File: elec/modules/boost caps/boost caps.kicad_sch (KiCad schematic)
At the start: 9 parts, among them J1 Conn_01x05, J2 Conn_01x05, U1 LM2587S-ADJ

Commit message: did boost without caps for now might have to re config stitch vias pos
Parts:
- removed J1, J2: Conn_01x05, Pinheaders:PinHeader_1x05_P2.54mm_Vertical, symbol Connector_Generic:Conn_01x05
- added C35: 0.1uF, Capacitor_SMD:C_0603_1608Metric, symbol Device:C
- added C36: 100uF, Capacitor_THT:CP_Radial_D8.0mm_P3.50mm, symbol Device:C_Polarized
- added C37, C38, C39, C41, C42, C43: 1000uF, Capacitor_THT:CP_Radial_D16.0mm_P7.50mm, symbol Device:C_Polarized
- added J1, J2, J3: Conn_01x01_Pin, cool custom thingy:custompadfat, symbol Connector:Conn_01x01_Pin
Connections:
- net +12V: now also C35.1, C36.1, J1.1 (Pin_1)
- net +24V: now also C37.1, C38.1, C39.1, C41.1, C42.1, C43.1, J2.1 (Pin_1)
- net GND: now also C35.2, C36.2, C37.2, C38.2, C39.2, C41.2, C42.2, C43.2, J3.1 (Pin_1)

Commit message: sleepy but did most pcbs
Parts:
- removed C35: 0.1uF, Capacitor_SMD:C_0603_1608Metric, symbol Device:C
- removed C36: 100uF, Capacitor_THT:CP_Radial_D8.0mm_P3.50mm, symbol Device:C_Polarized
- removed C40: 0.68uF, Capacitor_SMD:C_0603_1608Metric, symbol Device:C
- removed D2: MBR745, Package_TO_SOT_THT:TO-220-2_Vertical, symbol Diode:MBR745
- removed J1, J2, J3: Conn_01x01_Pin, cool custom thingy:custompadfat, symbol Connector:Conn_01x01_Pin
- removed L33: 33uH, Inductor_SMD:L_APV_APH1040, symbol Device:L
- removed R35: 36.9K/56k, Capacitor_SMD:C_0603_1608Metric, symbol Device:R
- removed R36: 2K/2.94k, Capacitor_SMD:C_0603_1608Metric, symbol Device:R
- removed R38: 3K, Capacitor_SMD:C_0603_1608Metric, symbol Device:R
- removed U1: LM2587S-ADJ, Boost:VREG_TPS79625KTTR, symbol lm2587(boost):LM2587S-ADJ
- added J1, J2: Conn_01x05, Pinheaders:PinHeader_1x05_P2.54mm_Vertical, symbol Connector_Generic:Conn_01x05
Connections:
- net +24V is gone; now on net +12V: C37.1, C38.1, C39.1, C41.1, C42.1, C43.1
- net +12V: now also J1.1 (Pin_1), J1.2 (Pin_2), J1.3 (Pin_3), J2.1 (Pin_1), J2.2 (Pin_2), J2.3 (Pin_3)
- net GND: now also J1.5 (Pin_5), J2.5 (Pin_5)
- no-connect marks 0 -> 2

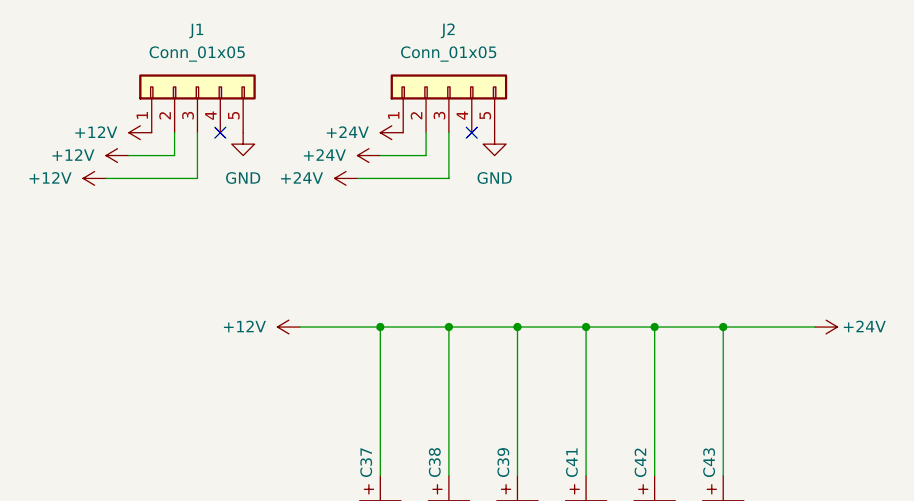
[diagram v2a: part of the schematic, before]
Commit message: finishe dcaps for boost
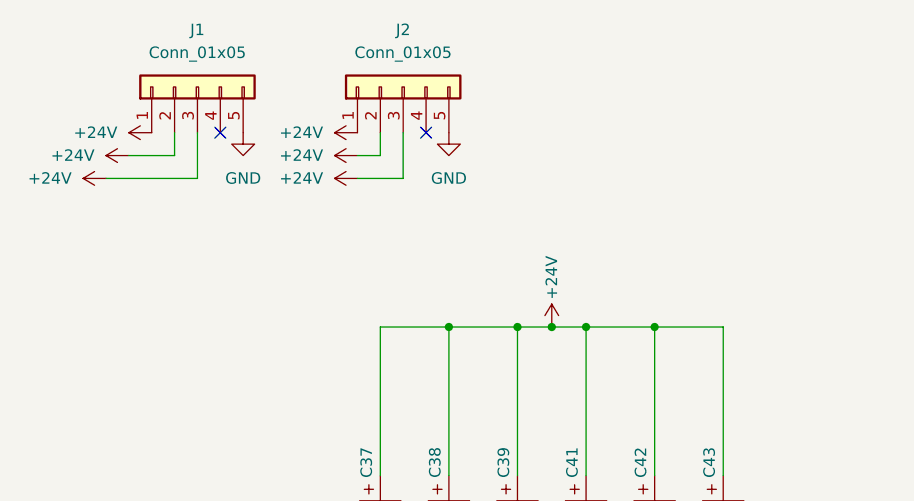
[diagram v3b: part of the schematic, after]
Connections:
- net +12V renamed +24V

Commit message: chore: boostcaps production files
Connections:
- net +24V: no longer J1.3 (Pin_3), J2.3 (Pin_3)
- net GND: now also J1.4 (Pin_4), J2.4 (Pin_4)
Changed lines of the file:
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@@
 	)
 	(no_connect
-		(at 177.8 49.53)
+		(at 152.4 49.53)
 	)
 	(no_connect
-		(at 154.94 49.53)
-	)
-	(wire
-		(pts
-			(xy 175.26 54.61) (xy 170.18 54.61)
-		)
-		(stroke
-			(width 0)
-			(type default)
-		)
+		(at 175.26 49.53)
 	)
 	(wire
@@
 	(wire
 		(pts
-			(xy 152.4 54.61) (xy 142.24 54.61)
-		)
-		(stroke
-			(width 0)
-			(type default)
-		)
-	)
-	(wire
-		(pts
-			(xy 152.4 49.53) (xy 152.4 54.61)
-		)
-		(stroke
-			(width 0)
-			(type default)
-		)
-	)
-	(wire
-		(pts
 			(xy 195.58 95.25) (xy 195.58 111.76)
 		)
@@
 		(pts
 			(xy 195.58 111.76) (xy 191.77 111.76)
-		)
-		(stroke
-			(width 0)
-			(type default)
-		)
-	)
-	(wire
-		(pts
-			(xy 175.26 49.53) (xy 175.26 54.61)
 		)
 		(stroke
@@
 				(path "/97baff51-d1b5-4933-bf19-f5d3c53b231d"
 					(reference "#PWR07")
+					(unit 1)
+				)
+			)
+		)
+	)
+	(symbol
+		(lib_id "power:GND")
+		(at 177.8 49.53 0)
+		(unit 1)
+		(exclude_from_sim no)
+		(in_bom yes)
+		(on_board yes)
+		(dnp no)
+		(fields_autoplaced yes)
+		(property "Reference" "#PWR08"
+			(at 177.8 55.88 0)
+			(effects
+				(font
+					(size 1.27 1.27)
+				)
+				(hide yes)
+			)
+		)
+		(property "Value" "GND"
+			(at 177.8 54.61 0)
+			(effects
+				(font
+					(size 1.27 1.27)
+				)
+			)
+		)
+		(property "Footprint" ""
+			(at 177.8 49.53 0)
+			(effects
+				(font
+					(size 1.27 1.27)
+				)
+				(hide yes)
+			)
+		)
+		(property "Datasheet" ""
+			(at 177.8 49.53 0)
+			(effects
+				(font
+					(size 1.27 1.27)
+				)
+				(hide yes)
+			)
+		)
+		(property "Description" "Power symbol creates a global label with name \"GND\" , ground"
+			(at 177.8 49.53 0)
+			(effects
+				(font
+					(size 1.27 1.27)
+				)
+				(hide yes)
+			)
+		)
+		(pin "1"
+		)
+		(instances
+			(project "boost caps"
+				(path "/97baff51-d1b5-4933-bf19-f5d3c53b231d"
+					(reference "#PWR08")
 					(unit 1)
 				)
@@
 	)
 	(symbol
-		(lib_id "power:+24V")
-		(at 142.24 54.61 90)
-		(unit 1)
-		(exclude_from_sim no)
-		(in_bom yes)
-		(on_board yes)
-		(dnp no)
-		(fields_autoplaced yes)
-		(property "Reference" "#PWR03"
-			(at 146.05 54.61 0)
-			(effects
-				(font
-					(size 1.27 1.27)
-				)
-				(hide yes)
-			)
-		)
-		(property "Value" "+24V"
-			(at 138.43 54.6099 90)
-			(effects
-				(font
-					(size 1.27 1.27)
-				)
-				(justify left)
-			)
-		)
-		(property "Footprint" ""
-			(at 142.24 54.61 0)
-			(effects
-				(font
-					(size 1.27 1.27)
-				)
-				(hide yes)
-			)
-		)
-		(property "Datasheet" ""
-			(at 142.24 54.61 0)
-			(effects
-				(font
-					(size 1.27 1.27)
-				)
-				(hide yes)
-			)
-		)
-		(property "Description" "Power symbol creates a global label with name \"+24V\""
-			(at 142.24 54.61 0)
-			(effects
-				(font
-					(size 1.27 1.27)
-				)
-				(hide yes)
-			)
-		)
-		(pin "1"
-		)
-		(instances
-			(project "boost caps"
-				(path "/97baff51-d1b5-4933-bf19-f5d3c53b231d"
-					(reference "#PWR03")
-					(unit 1)
-				)
-			)
-		)
-	)
-	(symbol
-		(lib_id "power:+24V")
-		(at 170.18 54.61 90)
-		(unit 1)
-		(exclude_from_sim no)
-		(in_bom yes)
-		(on_board yes)
-		(dnp no)
-		(fields_autoplaced yes)
-		(property "Reference" "#PWR08"
-			(at 173.99 54.61 0)
-			(effects
-				(font
-					(size 1.27 1.27)
-				)
-				(hide yes)
-			)
-		)
-		(property "Value" "+24V"
-			(at 166.37 54.6099 90)
-			(effects
-				(font
-					(size 1.27 1.27)
-				)
-				(justify left)
-			)
-		)
-		(property "Footprint" ""
-			(at 170.18 54.61 0)
-			(effects
-				(font
-					(size 1.27 1.27)
-				)
-				(hide yes)
-			)
-		)
-		(property "Datasheet" ""
-			(at 170.18 54.61 0)
-			(effects
-				(font
-					(size 1.27 1.27)
-				)
-				(hide yes)
-			)
-		)
-		(property "Description" "Power symbol creates a global label with name \"+24V\""
-			(at 170.18 54.61 0)
-			(effects
-				(font
-					(size 1.27 1.27)
-				)
-				(hide yes)
-			)
-		)
-		(pin "1"
-		)
-		(instances
-			(project "boost caps"
-				(path "/97baff51-d1b5-4933-bf19-f5d3c53b231d"
-					(reference "#PWR08")
-					(unit 1)
-				)
-			)
-		)
-	)
-	(symbol
 		(lib_id "Connector_Generic:Conn_01x05")
 		(at 152.4 44.45 90)
@@
 					(unit 1)
 				)
+			)
+		)
+	)
+	(symbol
+		(lib_id "power:GND")
+		(at 154.94 49.53 0)
+		(unit 1)
+		(exclude_from_sim no)
+		(in_bom yes)
+		(on_board yes)
+		(dnp no)
+		(fields_autoplaced yes)
+		(property "Reference" "#PWR03"
+			(at 154.94 55.88 0)
+			(effects
+				(font
+					(size 1.27 1.27)
+				)
+				(hide yes)
+			)
+		)
+		(property "Value" "GND"
+			(at 154.94 54.61 0)
+			(effects
+				(font
+					(size 1.27 1.27)
+				)
+			)
+		)
+		(property "Footprint" ""
+			(at 154.94 49.53 0)
+			(effects
+				(font
+					(size 1.27 1.27)
+				)
+				(hide yes)
+			)
+		)
+		(property "Datasheet" ""
+			(at 154.94 49.53 0)
+			(effects
+				(font
+					(size 1.27 1.27)
+				)
+				(hide yes)
+			)
+		)
+		(property "Description" "Power symbol creates a global label with name \"GND\" , ground"
+			(at 154.94 49.53 0)
+			(effects
+				(font
+					(size 1.27 1.27)
+				)
+				(hide yes)
+			)
+		)
+		(pin "1"
+		)
+		(instances
+			(project "boost caps"
+				(path "/97baff51-d1b5-4933-bf19-f5d3c53b231d"
+					(reference "#PWR03")
+					(unit 1)
+				)
